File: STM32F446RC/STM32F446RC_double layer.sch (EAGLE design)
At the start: 75 parts, among them IC1 STM32F446RCT6

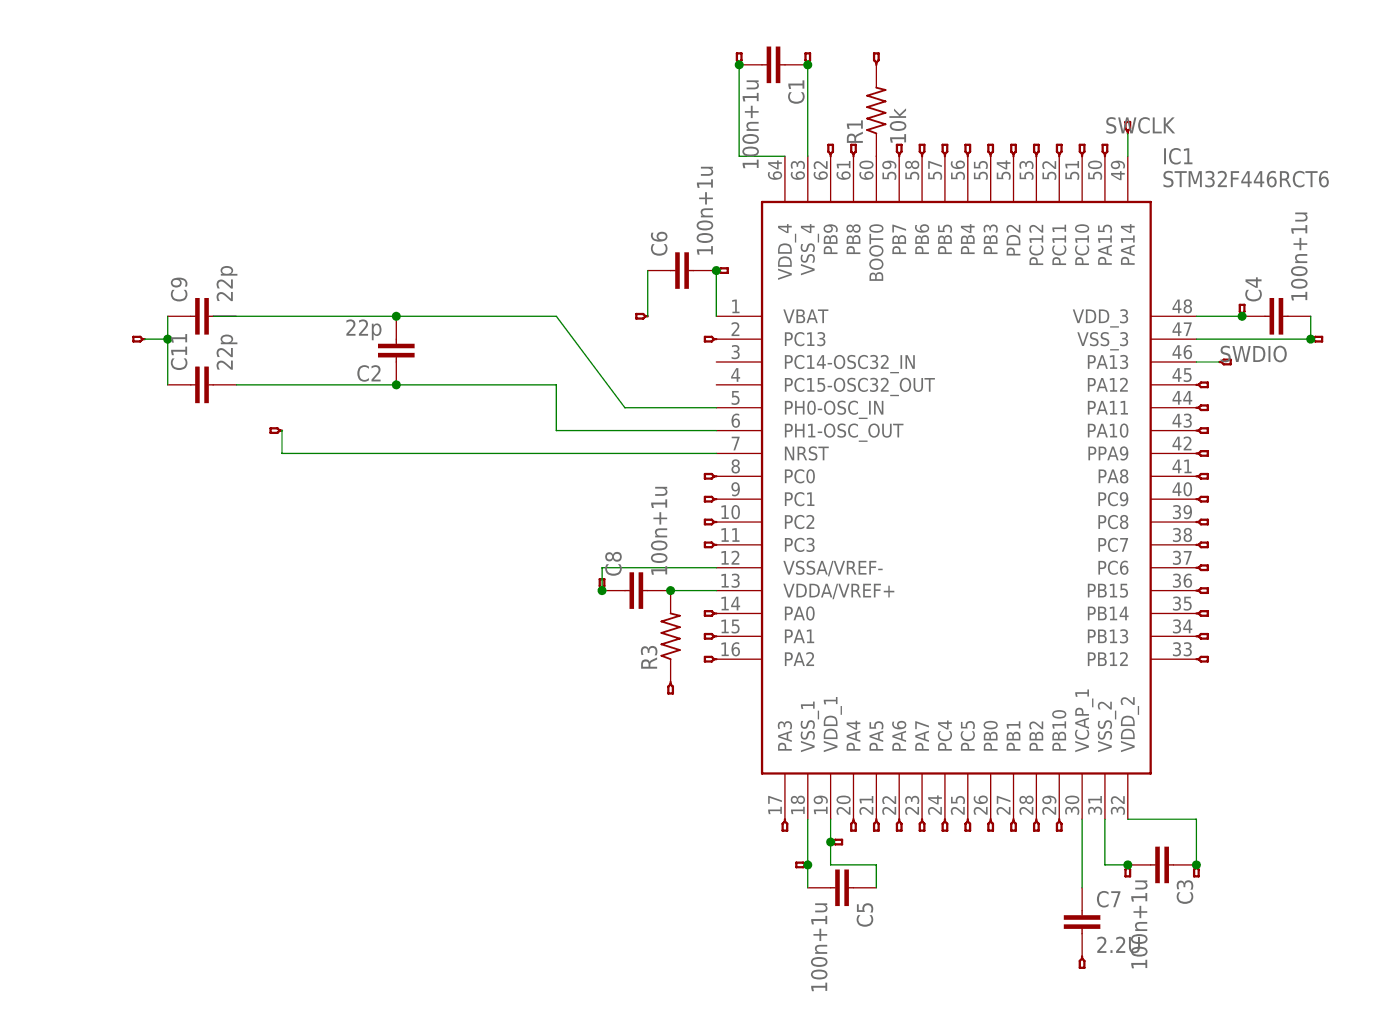
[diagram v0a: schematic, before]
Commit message: added double layer
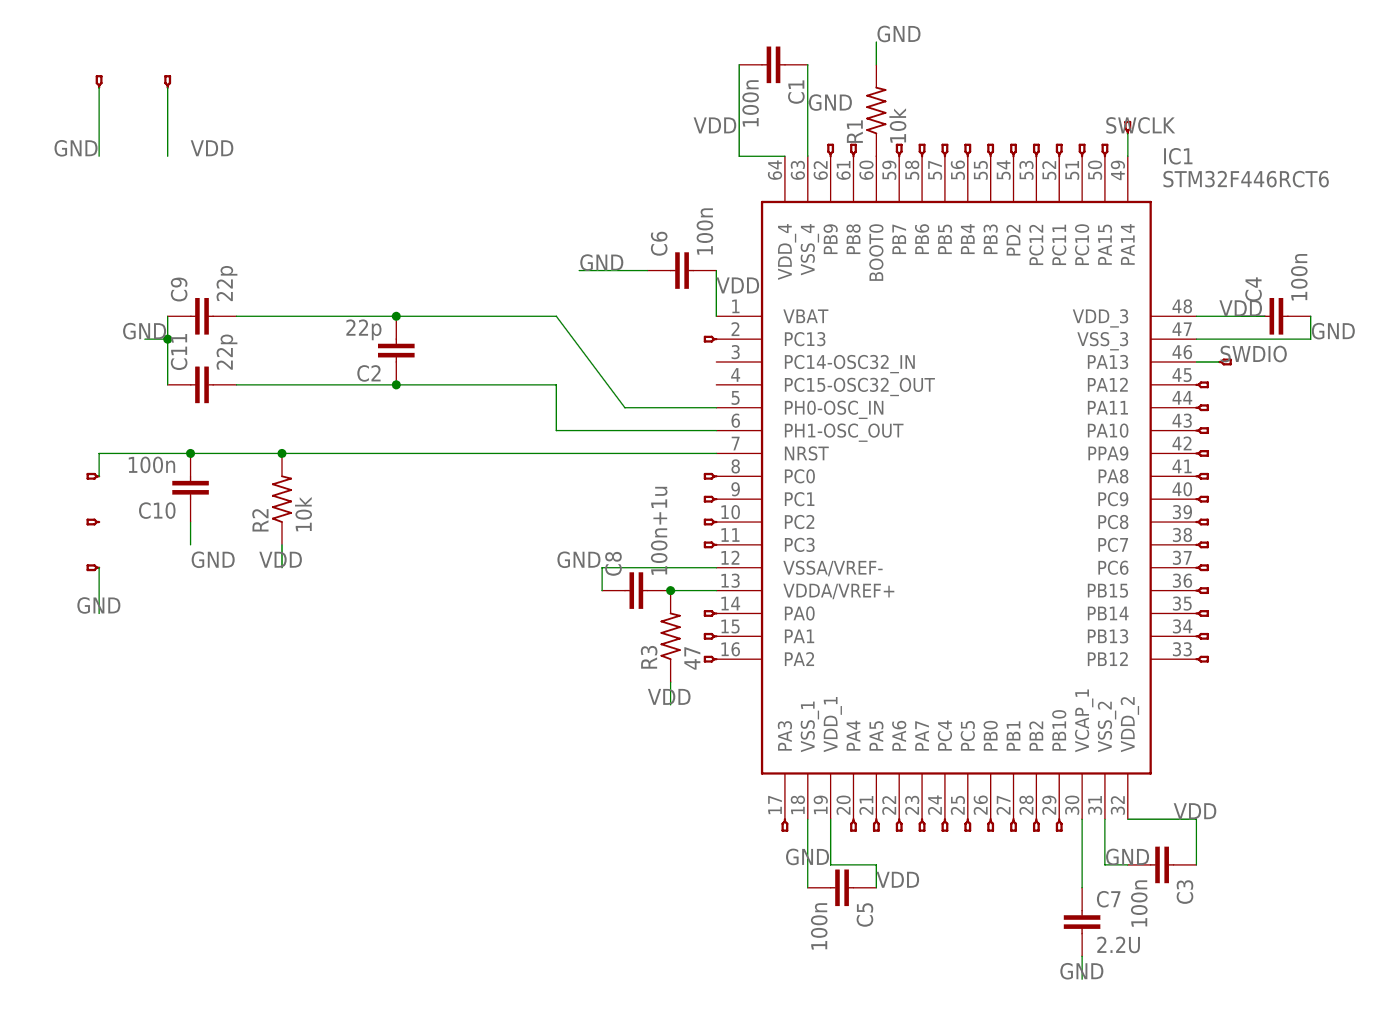
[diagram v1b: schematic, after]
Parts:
- removed JP50, JP51, JP52, JP53, JP56, JP57, JP58, JP59, JP61, JP62, JP63, JP65: (no value), F405Pill:HEADERHOLE-HEADERHOLE
- added C10: 100n, capacitor-wima:C2,5-3
- added JP8: (no value), F405Pill:HEADERHOLE-HEADERHOLE
- added R2: 10k, rcl:R-US_0204/2V
- C1, C3, C4, C5, C6: value 100n+1u -> 100n
- R3: value (none) -> 47
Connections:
- removed net N$1: C3.2, IC1.VSS_2, JP50.P$1
- removed net N$4: C5.2, IC1.VSS_1, JP20.P$1
- removed net N$54: C7.2, JP49.P$1
- removed net N$55: C3.1, IC1.VDD_2, JP51.P$1
- removed net N$56: C4.2, IC1.VSS_3, JP52.P$1
- removed net N$57: JP56.P$1, R1.2
- removed net N$58: C6.2, IC1.VBAT, JP7.P$1
- removed net N$59: C8.1, IC1.VSSA/VREF-, JP62.P$1
- removed net N$6: C1.2, IC1.VDD_4, JP58.P$1
- removed net N$60: JP61.P$1, R3.1
- removed net N$63: C11.1, C9.1, JP65.P$1
- removed net N$64: C5.1, IC1.VDD_1, JP48.P$1
- removed net N$67: C6.1, JP59.P$1
- removed net N$8: C1.1, IC1.VSS_4, JP57.P$1
- removed net N$89: C4.1, IC1.VDD_3, JP53.P$1
- new net GND: C1.1, C10.1, C11.1, C3.2, C4.2, C5.2, C6.1, C7.2, C8.1, C9.1, IC1.VSSA/VREF-, IC1.VSS_1, IC1.VSS_2, IC1.VSS_3, IC1.VSS_4, JP49.P$1, JP7.P$1, R1.2
- new net VDD: C1.2, C3.1, C4.1, C5.1, C6.2, IC1.VBAT, IC1.VDD_1, IC1.VDD_2, IC1.VDD_3, IC1.VDD_4, JP8.P$1, R2.1, R3.1
- net N$3: now also C10.2, JP20.P$1, R2.2; no longer JP63.P$1
- net N$53: now also C9.2

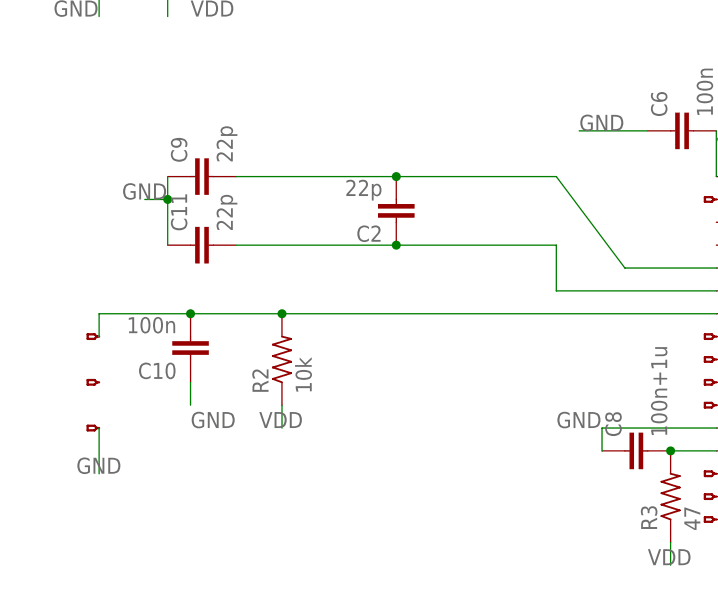
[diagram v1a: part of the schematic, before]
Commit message: added double layer
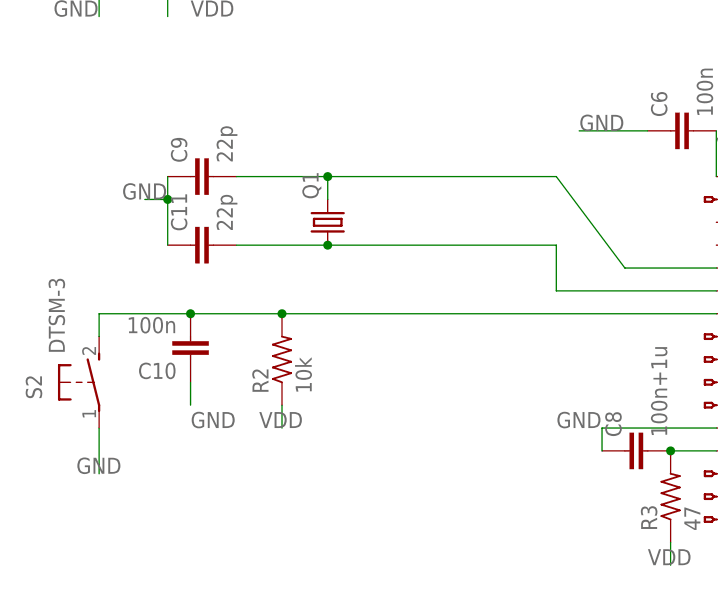
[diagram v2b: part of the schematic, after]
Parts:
- removed C2: 22p, capacitor-wima:C2,5-3
- removed JP20, JP48, JP49: (no value), F405Pill:HEADERHOLE-HEADERHOLE
- added Q1: (no value), crystal:CRYSTALHC49S
- added S2: DTSM-3, switch-tact:DTSM-3
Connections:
- net GND: now also S2.1; no longer JP49.P$1
- net N$3: now also S2.2; no longer JP20.P$1
- net N$53: now also Q1.2; no longer C2.2
- net N$7: now also Q1.1; no longer C2.1
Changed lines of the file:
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@@
 <part name="JP54" library="F405Pill" deviceset="HEADERHOLE" device="-HEADERHOLE"/>
 <part name="JP55" library="F405Pill" deviceset="HEADERHOLE" device="-HEADERHOLE"/>
-<part name="C2" library="capacitor-wima" library_urn="urn:adsk.eagle:library:116" deviceset="C" device="2,5-3" package3d_urn="urn:adsk.eagle:package:5436/1" value="22p"/>
 <part name="JP7" library="F405Pill" deviceset="HEADERHOLE" device="-HEADERHOLE"/>
 <part name="JP8" library="F405Pill" deviceset="HEADERHOLE" device="-HEADERHOLE"/>
 <part name="R2" library="rcl" library_urn="urn:adsk.eagle:library:334" deviceset="R-US_" device="0204/2V" package3d_urn="urn:adsk.eagle:package:23495/1" value="10k"/>
 <part name="C10" library="capacitor-wima" library_urn="urn:adsk.eagle:library:116" deviceset="C" device="2,5-3" package3d_urn="urn:adsk.eagle:package:5436/1" value="100n"/>
-<part name="JP20" library="F405Pill" deviceset="HEADERHOLE" device="-HEADERHOLE"/>
-<part name="JP48" library="F405Pill" deviceset="HEADERHOLE" device="-HEADERHOLE"/>
-<part name="JP49" library="F405Pill" deviceset="HEADERHOLE" device="-HEADERHOLE"/>
+<part name="Q1" library="crystal" library_urn="urn:adsk.eagle:library:204" deviceset="CRYSTAL" device="HC49S" package3d_urn="urn:adsk.eagle:package:12071/1"/>
+<part name="S2" library="switch-tact" deviceset="DTSM-3" device=""/>
 </parts>
 <sheets>
@@
 <attribute name="VALUE" x="75.692" y="83.82" size="0.4064" layer="96" ratio="10" rot="R90"/>
 </instance>
-<instance part="C2" gate="G$1" x="-5.08" y="58.42" rot="R180">
-<attribute name="NAME" x="-6.604" y="58.039" size="1.778" layer="95" rot="R180"/>
-<attribute name="VALUE" x="-6.604" y="63.119" size="1.778" layer="96" rot="R180"/>
-</instance>
 <instance part="JP7" gate="G$1" x="-38.1" y="88.9" rot="R270">
 <attribute name="VALUE" x="-38.608" y="88.9" size="0.4064" layer="96" ratio="10" rot="R90"/>
@@
 <attribute name="VALUE" x="-29.464" y="47.879" size="1.778" layer="96" rot="R180"/>
 </instance>
-<instance part="JP20" gate="G$1" x="-38.1" y="45.72">
-<attribute name="VALUE" x="-38.1" y="45.212" size="0.4064" layer="96" ratio="10" rot="R180"/>
-</instance>
-<instance part="JP48" gate="G$1" x="-38.1" y="40.64">
-<attribute name="VALUE" x="-38.1" y="40.132" size="0.4064" layer="96" ratio="10" rot="R180"/>
-</instance>
-<instance part="JP49" gate="G$1" x="-38.1" y="35.56">
-<attribute name="VALUE" x="-38.1" y="35.052" size="0.4064" layer="96" ratio="10" rot="R180"/>
+<instance part="Q1" gate="G$1" x="-12.7" y="58.42" rot="R90">
+<attribute name="NAME" x="-13.716" y="60.96" size="1.778" layer="95" rot="R90"/>
+<attribute name="VALUE" x="-10.16" y="60.96" size="1.778" layer="96" rot="R90"/>
+</instance>
+<instance part="S2" gate="G$1" x="-38.1" y="40.64">
+<attribute name="NAME" x="-44.45" y="38.735" size="1.778" layer="95" rot="R90"/>
+<attribute name="VALUE" x="-41.91" y="43.815" size="1.778" layer="96" rot="R90"/>
 </instance>
 </instances>
@@
 <wire x1="30.48" y1="50.8" x2="12.7" y2="50.8" width="0.1524" layer="91"/>
 <wire x1="12.7" y1="50.8" x2="12.7" y2="55.88" width="0.1524" layer="91"/>
-<pinref part="C2" gate="G$1" pin="1"/>
-<wire x1="-5.08" y1="55.88" x2="12.7" y2="55.88" width="0.1524" layer="91"/>
+<wire x1="-12.7" y1="55.88" x2="12.7" y2="55.88" width="0.1524" layer="91"/>
 <pinref part="C11" gate="G$1" pin="2"/>
-<wire x1="-5.08" y1="55.88" x2="-22.86" y2="55.88" width="0.1524" layer="91"/>
-<junction x="-5.08" y="55.88"/>
+<pinref part="Q1" gate="G$1" pin="1"/>
+<wire x1="-12.7" y1="55.88" x2="-22.86" y2="55.88" width="0.1524" layer="91"/>
+<junction x="-12.7" y="55.88"/>
 </segment>
 </net>
@@
 <wire x1="30.48" y1="53.34" x2="20.32" y2="53.34" width="0.1524" layer="91"/>
 <wire x1="20.32" y1="53.34" x2="12.7" y2="63.5" width="0.1524" layer="91"/>
-<pinref part="C2" gate="G$1" pin="2"/>
-<wire x1="12.7" y1="63.5" x2="-5.08" y2="63.5" width="0.1524" layer="91"/>
 <pinref part="C9" gate="G$1" pin="2"/>
-<wire x1="-5.08" y1="63.5" x2="-22.86" y2="63.5" width="0.1524" layer="91"/>
-<junction x="-5.08" y="63.5"/>
+<wire x1="12.7" y1="63.5" x2="-12.7" y2="63.5" width="0.1524" layer="91"/>
+<pinref part="Q1" gate="G$1" pin="2"/>
+<wire x1="-12.7" y1="63.5" x2="-22.86" y2="63.5" width="0.1524" layer="91"/>
+<wire x1="-12.7" y1="60.96" x2="-12.7" y2="63.5" width="0.1524" layer="91"/>
+<junction x="-12.7" y="63.5"/>
 </segment>
 </net>
@@
 <wire x1="-38.1" y1="35.56" x2="-38.1" y2="30.48" width="0.1524" layer="91"/>
 <label x="-40.64" y="30.48" size="1.778" layer="95"/>
-<pinref part="JP49" gate="G$1" pin="P$1"/>
+<pinref part="S2" gate="G$1" pin="1"/>
 </segment>
 </net>
@@
 <pinref part="C10" gate="G$1" pin="2"/>
 <junction x="-27.94" y="48.26"/>
-<pinref part="JP20" gate="G$1" pin="P$1"/>
-</segment>
-</net>
+<pinref part="S2" gate="G$1" pin="2"/>
+</segment>
+</net>
